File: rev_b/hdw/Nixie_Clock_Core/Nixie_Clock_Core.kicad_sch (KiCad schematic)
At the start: 0 parts

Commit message: lots of rev B control board schematic progress
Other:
- removed sheet USB Telemetry
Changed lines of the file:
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@@
-    )
-  )
-  (sheet (at 33.02 149.86) (size 12.7 3.81) (fields_autoplaced)
-    (stroke (width 0.1524) (type solid))
-    (fill (color 0 0 0 0.0000))
-    (property "Sheetname" "USB Telemetry" (at 33.02 149.1484 0)
-      (effects (font (size 1.27 1.27)) (justify left bottom))
-    )
-    (property "Sheetfile" "USB_Telemetry.kicad_sch" (at 33.02 154.2546 0)
-      (effects (font (size 1.27 1.27)) (justify left top))
-    )
-    (instances
-      (project "Nixie_Clock_Core"
-        (path "/16fdce21-b570-4d81-a458-e8839d611806" (page "14"))
-      )
     )
   )
@@
     )
   )
-  (sheet (at 33.02 170.18) (size 12.7 3.81) (fields_autoplaced)
+  (sheet (at 33.02 160.02) (size 12.7 3.81) (fields_autoplaced)
     (stroke (width 0.1524) (type solid))
     (fill (color 0 0 0 0.0000))
-    (property "Sheetname" "PGOOD LEDs" (at 33.02 169.4684 0)
+    (property "Sheetname" "PGOOD LEDs" (at 33.02 159.3084 0)
       (effects (font (size 1.27 1.27)) (justify left bottom))
     )
-    (property "Sheetfile" "PGOOD_LEDs.kicad_sch" (at 33.02 174.5746 0)
+    (property "Sheetfile" "PGOOD_LEDs.kicad_sch" (at 33.02 164.4146 0)
       (effects (font (size 1.27 1.27)) (justify left top))
     )
@@
     )
   )
-  (sheet (at 33.02 160.02) (size 12.7 3.81) (fields_autoplaced)
+  (sheet (at 33.02 149.86) (size 12.7 3.81) (fields_autoplaced)
     (stroke (width 0.1524) (type solid))
     (fill (color 0 0 0 0.0000))
-    (property "Sheetname" "Platform ETC" (at 33.02 159.3084 0)
+    (property "Sheetname" "Platform ETC" (at 33.02 149.1484 0)
       (effects (font (size 1.27 1.27)) (justify left bottom))
     )
-    (property "Sheetfile" "Platform_ETC.kicad_sch" (at 33.02 164.4146 0)
+    (property "Sheetfile" "Platform_ETC.kicad_sch" (at 33.02 154.2546 0)
       (effects (font (size 1.27 1.27)) (justify left top))
     )
@@
     )
   )
-  (sheet (at 33.02 180.34) (size 12.7 3.81) (fields_autoplaced)
+  (sheet (at 33.02 170.18) (size 12.7 3.81) (fields_autoplaced)
     (stroke (width 0.1524) (type solid))
     (fill (color 0 0 0 0.0000))
-    (property "Sheetname" "Status LEDs" (at 33.02 179.6284 0)
+    (property "Sheetname" "Status LEDs" (at 33.02 169.4684 0)
       (effects (font (size 1.27 1.27)) (justify left bottom))
     )
-    (property "Sheetfile" "Status_LEDs.kicad_sch" (at 33.02 184.7346 0)
+    (property "Sheetfile" "Status_LEDs.kicad_sch" (at 33.02 174.5746 0)
       (effects (font (size 1.27 1.27)) (justify left top))
     )

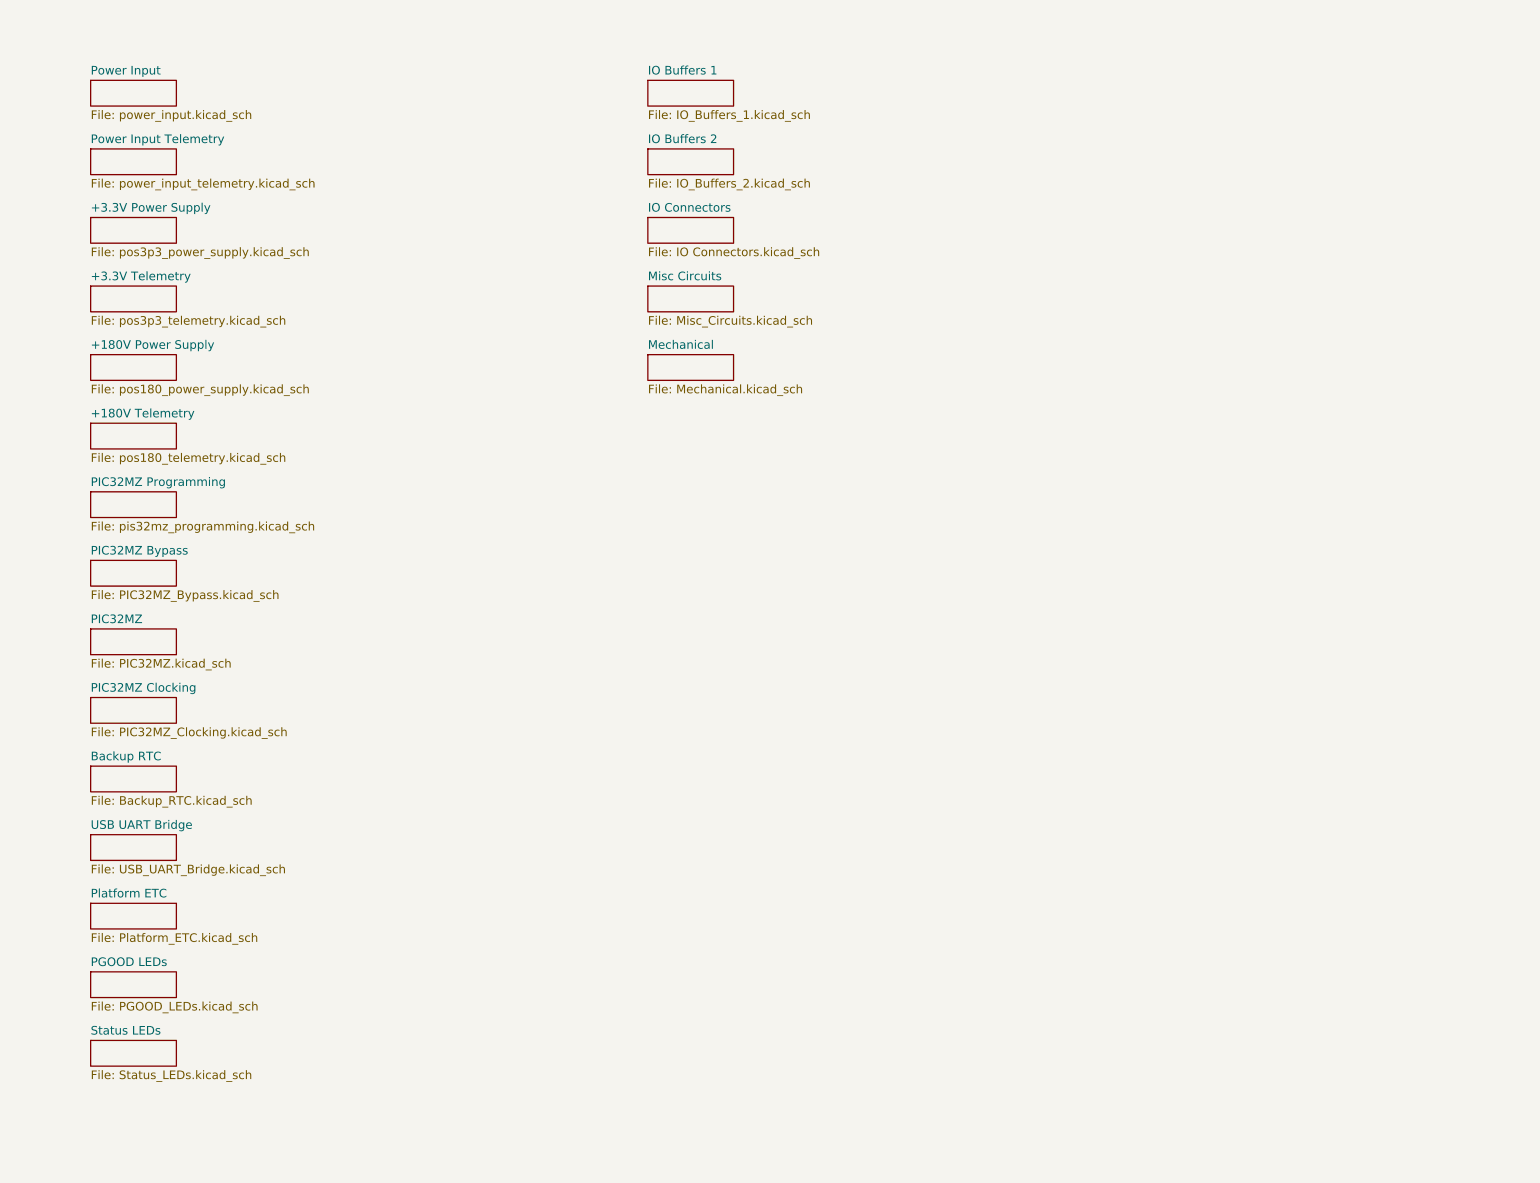
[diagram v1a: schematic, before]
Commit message: revamped POS180 telemetry
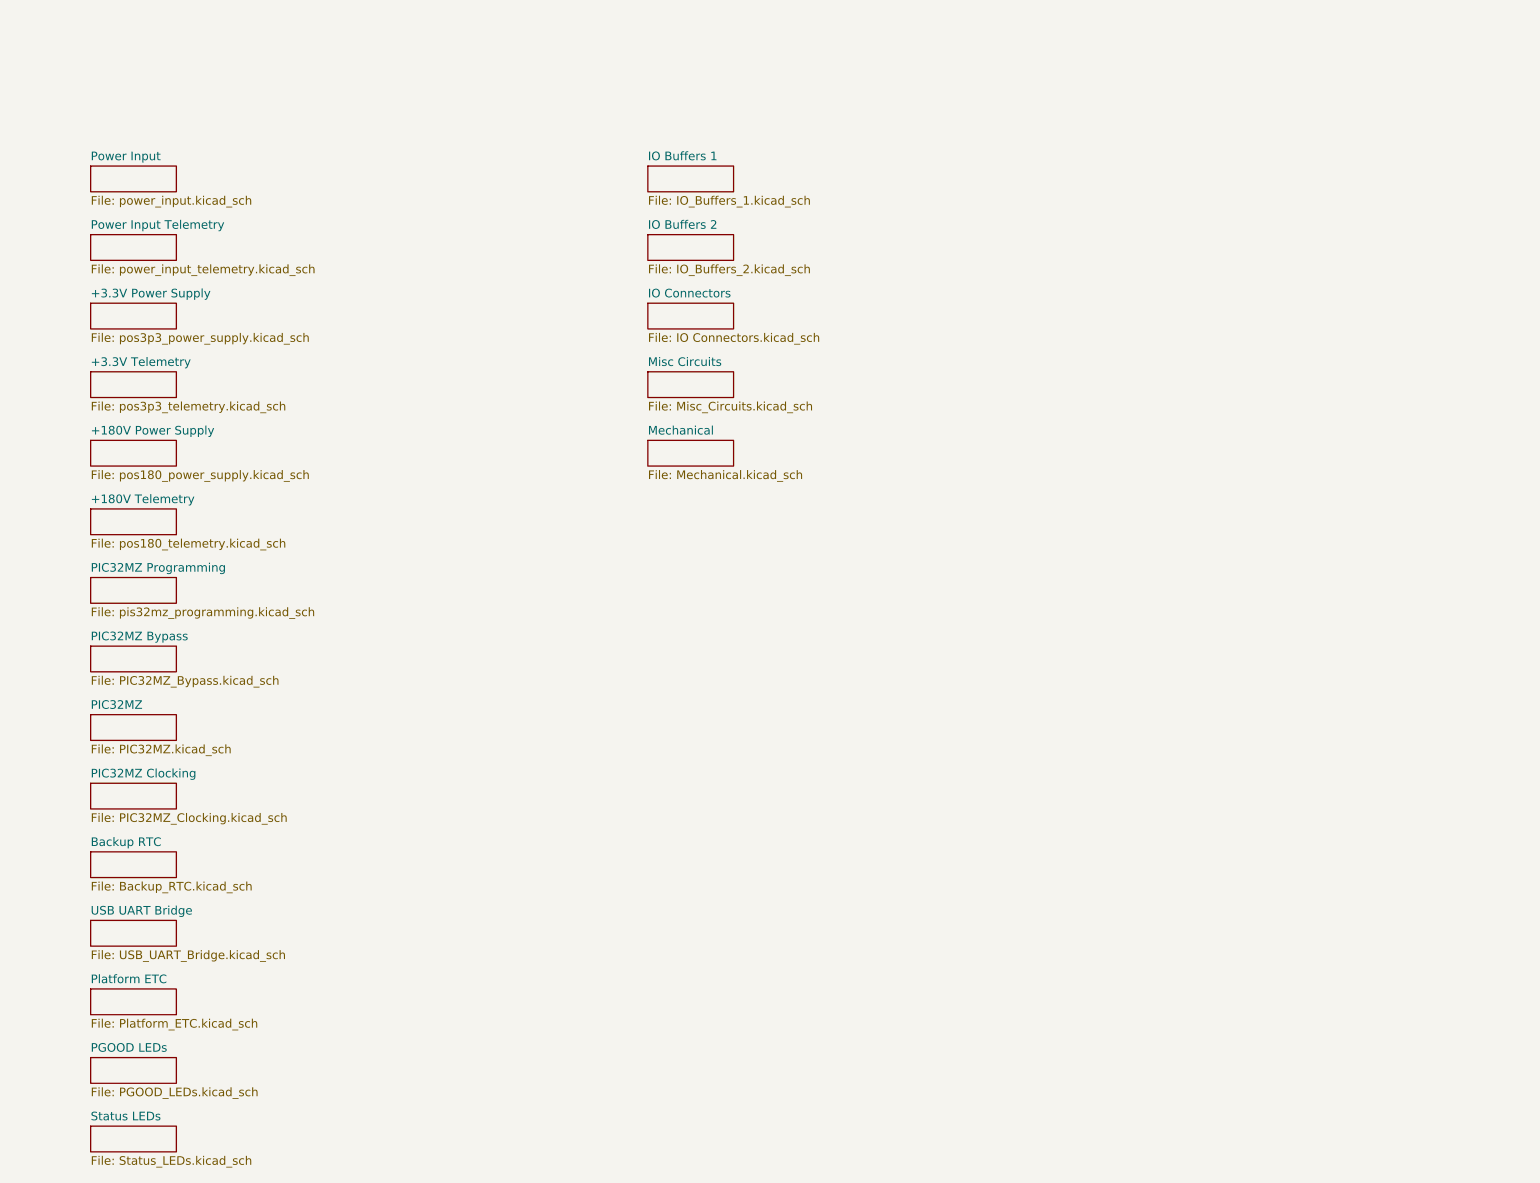
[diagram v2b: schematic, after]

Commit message: more schematic progress, assigning signals to MCU"
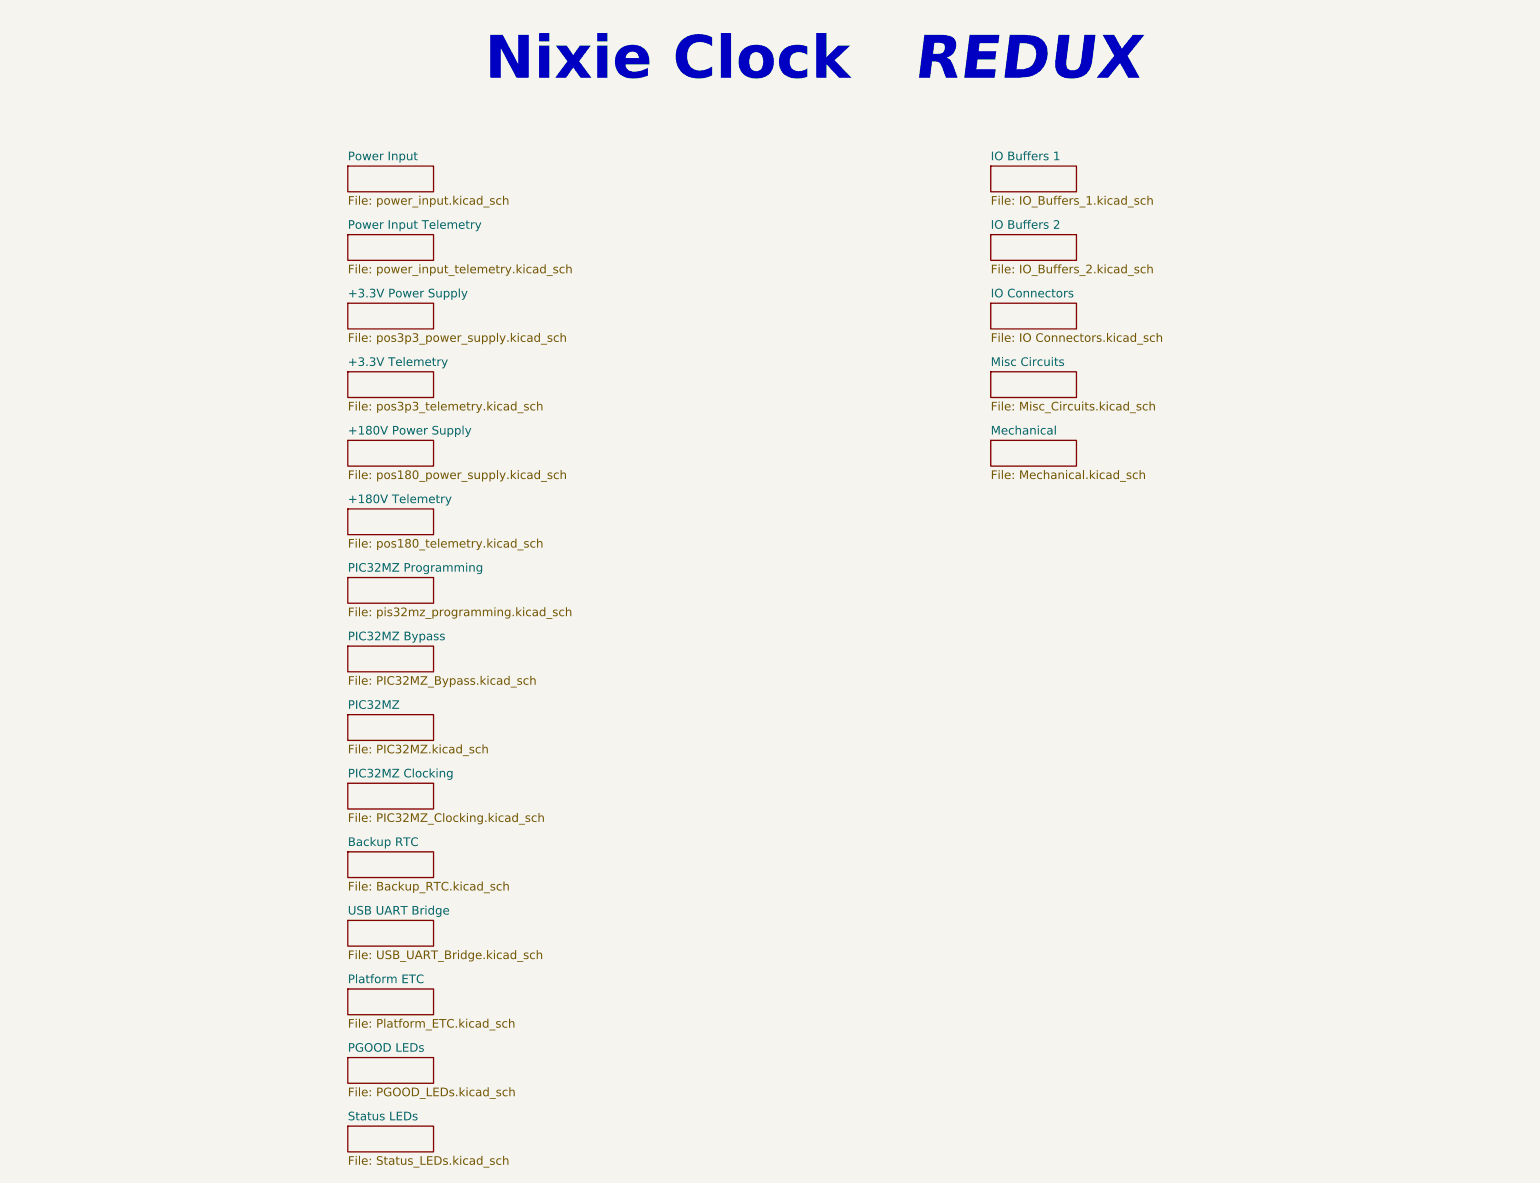
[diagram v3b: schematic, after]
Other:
- note added: "Nixie Clock"
- note added: "REDUX"

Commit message: hid all passive refdes on core PCB
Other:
- note added: "02. Power Input"
- note added: "03. Power Input Telemetry"
- note added: "04. +3.3V Power Supply"
- note added: "05. +3.3V Telemetry"
- note added: "06. +180V Power Supply"
- note added: "07. +180V Telemetry"
- note added: "08. PIC32MZ Programming"
- note added: "09. PIC32MZ Bypass"
- note added: "10. PIC32MZ"
- note added: "11. PIC32MZ Clocking"
- note added: "12. Backup RTC"
- note added: "13. USB UART Bridge"
- note added: "14. Platform ETC"
- note added: "15. PGOOD LEDs"
- note added: "16. Status LEDs"
- note added: "17. IO Buffers 1"
- note added: "18. IO Buffers 2"
- note added: "19. IO Connector"
- note added: "20. Misc Circuits"
- note added: "21. Mechanical"
- note added: "Nixie Clock - Core Board"
- note removed: "Nixie Clock"

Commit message: added BOM
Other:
- title: (none) -> Nixie Clock Redux Core Board
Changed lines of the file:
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@@
   (paper "A")
   (title_block
-    (date "2023-05-12")
-    (rev "PRELIM")
+    (title "Nixie Clock Redux Core Board")
+    (date "2023-07-30")
+    (rev "B")
     (company "Drew Maatman")
   )
